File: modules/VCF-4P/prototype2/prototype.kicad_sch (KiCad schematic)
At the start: 37 parts, among them J1 Conn_01x09, U1 TL074, U2 SSI2140

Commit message: VCF-4P: prototype2 - get cutoff CV from bus
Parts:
- removed RV1: 100K, -lmp-misc:Potentiometer_Bourns_3310R_Top, symbol -lmp:R_POT_TRIM
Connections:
- net BUS-CV: now also R1.1
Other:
- note added: "TODO: Increase this to see if it fixes square wave resonance"
- note removed: "TODO: Adjust for gain & overdrive"
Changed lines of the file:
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@@
-    (stroke (width 0) (type default) (color 0 0 0 0))
-  )
-  (wire (pts (xy 39.37 137.16) (xy 39.37 138.43))
     (stroke (width 0) (type default) (color 0 0 0 0))
   )
@@
   )
   (wire (pts (xy 100.33 58.42) (xy 100.33 59.69))
-    (stroke (width 0) (type default) (color 0 0 0 0))
-  )
-  (wire (pts (xy 39.37 146.05) (xy 39.37 147.32))
     (stroke (width 0) (type default) (color 0 0 0 0))
   )
@@
     (effects (font (size 1.27 1.27)) (justify left bottom))
   )
-  (text "TODO: Adjust for \ngain & overdrive" (at 67.31 33.02 0)
+  (text "TODO: Increase this \nto see if it fixes \nsquare wave resonance"
+    (at 67.31 33.02 0)
     (effects (font (size 1.27 1.27)) (justify left bottom))
   )
@@
     (effects (font (size 1.27 1.27)) (justify left bottom))
   )
-  (global_label "BUS-CV" (shape bidirectional) (at 134.62 88.9 0) (fields_autoplaced)
+  (global_label "BUS-CV" (shape output) (at 134.62 88.9 0) (fields_autoplaced)
     (effects (font (size 1.27 1.27)) (justify left))
-    (property "Intersheet References" "${INTERSHEET_REFS}" (id 0) (at 7.62 3.81 0)
-      (effects (font (size 1.27 1.27)) hide)
-    )
-  )
-  (global_label "BUS-GATE" (shape bidirectional) (at 134.62 86.36 0) (fields_autoplaced)
+    (property "Intersheet References" "${INTERSHEET_REFS}" (id 0) (at 144.6852 88.8206 0)
+      (effects (font (size 1.27 1.27)) (justify left) hide)
+    )
+  )
+  (global_label "BUS-GATE" (shape output) (at 134.62 86.36 0) (fields_autoplaced)
     (effects (font (size 1.27 1.27)) (justify left))
-    (property "Intersheet References" "${INTERSHEET_REFS}" (id 0) (at 7.62 3.81 0)
-      (effects (font (size 1.27 1.27)) hide)
+    (property "Intersheet References" "${INTERSHEET_REFS}" (id 0) (at 146.8018 86.2806 0)
+      (effects (font (size 1.27 1.27)) (justify left) hide)
     )
   )
@@
     (effects (font (size 1.27 1.27)) (justify right))
     (property "Intersheet References" "${INTERSHEET_REFS}" (id 0) (at 27.1277 39.2906 0)
+      (effects (font (size 1.27 1.27)) (justify right) hide)
+    )
+  )
+  (global_label "BUS-CV" (shape input) (at 43.18 142.24 180) (fields_autoplaced)
+    (effects (font (size 1.27 1.27)) (justify right))
+    (property "Intersheet References" "${INTERSHEET_REFS}" (id 0) (at 33.1148 142.1606 0)
       (effects (font (size 1.27 1.27)) (justify right) hide)
     )
@@
     (pin "11")
     (pin "4")
-  )
-  (symbol (lib_id "-lmp:R_POT_TRIM") (at 39.37 142.24 0) (mirror x) (unit 1)
-    (in_bom yes) (on_board yes) (fields_autoplaced)
-    (property "Reference" "RV1" (id 0) (at 37.5921 140.1369 0)
-      (effects (font (size 1.27 1.27)) (justify right))
-    )
-    (property "Value" "100K" (id 1) (at 37.5921 142.6738 0)
-      (effects (font (size 1.27 1.27)) (justify right))
-    )
-    (property "Footprint" "-lmp-misc:Potentiometer_Bourns_3310R_Top" (id 2) (at 39.37 142.24 0)
-      (effects (font (size 1.27 1.27)) hide)
-    )
-    (property "Datasheet" "https://www.mouser.ca/datasheet/2/54/3386-776606.pdf" (id 3) (at 39.37 142.24 0)
-      (effects (font (size 1.27 1.27)) hide)
-    )
-    (property "Label" "CUTOFF" (id 4) (at 37.5921 145.2107 0)
-      (effects (font (size 1.27 1.27)) (justify right))
-    )
-    (property "Manufacturer" "Bourns" (id 5) (at 39.37 142.24 0)
-      (effects (font (size 1.27 1.27)) hide)
-    )
-    (property "ManufacturerPartNum" "3386*" (id 6) (at 39.37 142.24 0)
-      (effects (font (size 1.27 1.27)) hide)
-    )
-    (property "Distributor" "Mouser" (id 7) (at 39.37 142.24 0)
-      (effects (font (size 1.27 1.27)) hide)
-    )
-    (property "DistributorPartNum" "652-3386*" (id 8) (at 39.37 142.24 0)
-      (effects (font (size 1.27 1.27)) hide)
-    )
-    (property "DistributorPartLink" "https://www.mouser.ca/c/passive-components/resistors/variable-resistors/trimmer-resistors-through-hole/?number+of+turns=1&series=3386&instock=y" (id 9) (at 39.37 142.24 0)
-      (effects (font (size 1.27 1.27)) hide)
-    )
-    (pin "1")
-    (pin "2")
-    (pin "3")
   )
   (symbol (lib_id "-lmp:R_1%_0W166") (at 198.12 107.95 0) (unit 1)
@@
     (pin "2")
   )
-  (symbol (lib_id "-lmp-power:+12V") (at 39.37 137.16 0) (unit 1)
-    (in_bom yes) (on_board yes) (fields_autoplaced)
-    (property "Reference" "#PWR07" (id 0) (at 39.37 140.97 0)
-      (effects (font (size 1.27 1.27)) hide)
-    )
-    (property "Value" "+12V" (id 1) (at 39.37 133.5842 0))
-    (property "Footprint" "" (id 2) (at 39.37 137.16 0)
-      (effects (font (size 1.27 1.27)) hide)
-    )
-    (property "Datasheet" "" (id 3) (at 39.37 137.16 0)
-      (effects (font (size 1.27 1.27)) hide)
-    )
-    (pin "1")
-  )
   (symbol (lib_id "-lmp-power:GND") (at 121.92 148.59 0) (unit 1)
     (in_bom yes) (on_board yes) (fields_autoplaced)
@@
     (pin "1")
     (pin "2")
-  )
-  (symbol (lib_id "-lmp-power:GND") (at 39.37 147.32 0) (unit 1)
-    (in_bom yes) (on_board yes) (fields_autoplaced)
-    (property "Reference" "#PWR08" (id 0) (at 39.37 153.67 0)
-      (effects (font (size 1.27 1.27)) hide)
-    )
-    (property "Value" "GND" (id 1) (at 39.37 151.7634 0))
-    (property "Footprint" "" (id 2) (at 39.37 147.32 0)
-      (effects (font (size 1.27 1.27)) hide)
-    )
-    (property "Datasheet" "" (id 3) (at 39.37 147.32 0)
-      (effects (font (size 1.27 1.27)) hide)
-    )
-    (pin "1")
   )
   (symbol (lib_id "-lmp-synth:SSI2140") (at 222.25 41.91 0) (unit 4)
@@
       (reference "#PWR06") (unit 1) (value "-12V") (footprint "")
     )
-    (path "/71142ee8-9f39-4bb4-b70d-32261bf87f71"
-      (reference "#PWR07") (unit 1) (value "+12V") (footprint "")
-    )
-    (path "/96bd24d1-a18b-4fe1-bb89-18daf1bebf18"
-      (reference "#PWR08") (unit 1) (value "GND") (footprint "")
-    )
     (path "/84d56833-5712-4fbf-9196-b496586e82ab"
       (reference "#PWR09") (unit 1) (value "+12V") (footprint "")
@@
       (reference "R26") (unit 1) (value "10K") (footprint "-lmp-stripboard:SB_Gen_2")
     )
-    (path "/11baca3c-c206-4892-9f9f-c61e2f2a6c00"
-      (reference "RV1") (unit 1) (value "100K") (footprint "-lmp-misc:Potentiometer_Bourns_3310R_Top")
-    )
     (path "/3d155eaf-f195-466b-907a-c2cc1c99b6ea"

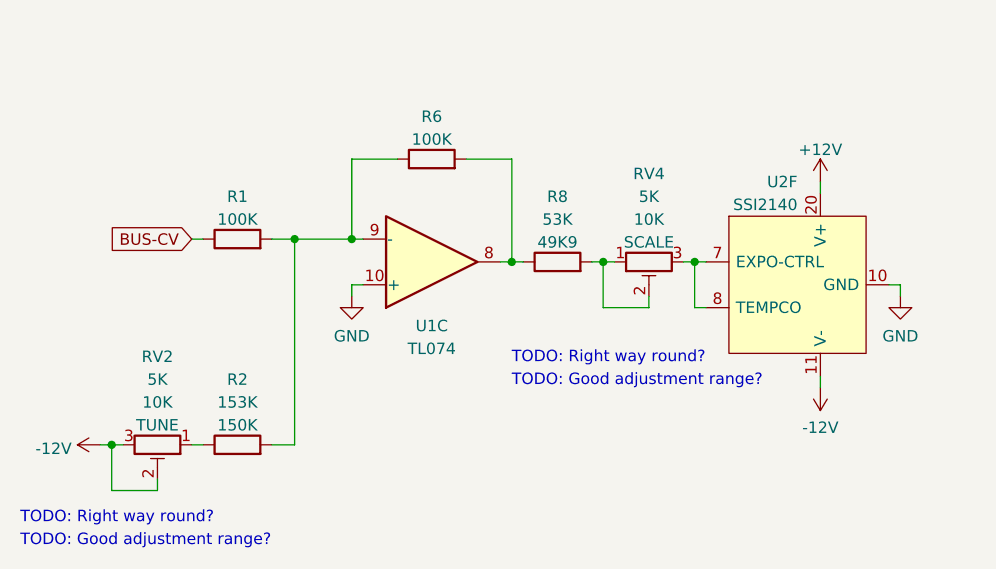
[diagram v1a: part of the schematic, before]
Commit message: VCF-4P: Calibration adjustments
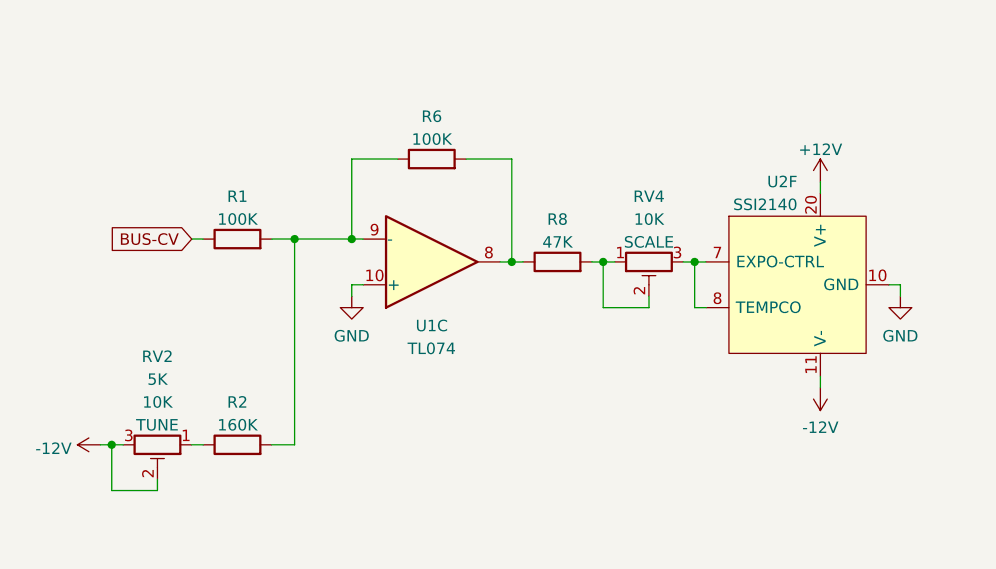
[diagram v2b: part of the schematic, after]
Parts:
- R2: value 153K -> 160K; Value2 150K -> (none)
- R8: value 53K -> 47K; Value2 49K9 -> (none)
- RV4: value 5K -> 10K; Value2 10K -> (none)
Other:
- note removed: "TODO: Good adjustment range?"
- note removed: "TODO: Right way round?"
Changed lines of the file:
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@@
     (stroke (width 0) (type default) (color 0 0 0 0))
-  )
-  (text "TODO: Good adjustment range?" (at 24.13 176.53 0)
-    (effects (font (size 1.27 1.27)) (justify left bottom))
-  )
-  (text "TODO: Right way round?" (at 78.74 156.21 0)
-    (effects (font (size 1.27 1.27)) (justify left bottom))
-  )
-  (text "TODO: Good adjustment range?" (at 78.74 158.75 0)
-    (effects (font (size 1.27 1.27)) (justify left bottom))
   )
   (text "TODO: Increase this \nto see if it fixes \nsquare wave resonance"
     (at 67.31 33.02 0)
-    (effects (font (size 1.27 1.27)) (justify left bottom))
-  )
-  (text "TODO: Right way round?" (at 24.13 173.99 0)
     (effects (font (size 1.27 1.27)) (justify left bottom))
   )
@@
   (symbol (lib_id "-lmp:R_1%_0W166") (at 83.82 144.78 90) (unit 1)
     (in_bom yes) (on_board yes) (fields_autoplaced)
-    (property "Reference" "R8" (id 0) (at 83.82 137.5274 90))
-    (property "Value" "53K" (id 1) (at 83.82 140.0643 90))
+    (property "Reference" "R8" (id 0) (at 83.82 140.0642 90))
+    (property "Value" "47K" (id 1) (at 83.82 142.6011 90))
     (property "Footprint" "-lmp-misc:R_Axial_DIN0207_L6.3mm_D2.5mm_P7.62mm_Horizontal" (id 2) (at 83.82 146.558 90)
       (effects (font (size 1.27 1.27)) hide)
@@
       (effects (font (size 1.27 1.27)) hide)
     )
-    (property "Value2" "49K9" (id 9) (at 83.82 142.6012 90))
     (pin "1")
     (pin "2")
@@
   (symbol (lib_id "-lmp:R_POT_TRIM") (at 93.98 144.78 90) (mirror x) (unit 1)
     (in_bom yes) (on_board yes) (fields_autoplaced)
-    (property "Reference" "RV4" (id 0) (at 93.98 134.9904 90))
-    (property "Value" "5K" (id 1) (at 93.98 137.5273 90))
+    (property "Reference" "RV4" (id 0) (at 93.98 137.5274 90))
+    (property "Value" "10K" (id 1) (at 93.98 140.0643 90))
     (property "Footprint" "-lmp-misc:Potentiometer_Bourns_3310R_Top" (id 2) (at 93.98 144.78 0)
       (effects (font (size 1.27 1.27)) hide)
@@
       (effects (font (size 1.27 1.27)) hide)
     )
-    (property "Value2" "10K" (id 10) (at 93.98 140.0642 90))
-    (property "Label" "SCALE" (id 4) (at 93.98 142.6011 90))
+    (property "Label" "SCALE" (id 4) (at 93.98 142.6012 90))
     (property "Manufacturer" "Bourns" (id 5) (at 93.98 144.78 0)
       (effects (font (size 1.27 1.27)) hide)
@@
   (symbol (lib_id "-lmp:R_1%_0W166") (at 48.26 165.1 90) (unit 1)
     (in_bom yes) (on_board yes) (fields_autoplaced)
-    (property "Reference" "R2" (id 0) (at 48.26 157.8474 90))
-    (property "Value" "153K" (id 1) (at 48.26 160.3843 90))
+    (property "Reference" "R2" (id 0) (at 48.26 160.3842 90))
+    (property "Value" "160K" (id 1) (at 48.26 162.9211 90))
     (property "Footprint" "-lmp-misc:R_Axial_DIN0207_L6.3mm_D2.5mm_P7.62mm_Horizontal" (id 2) (at 48.26 166.878 90)
       (effects (font (size 1.27 1.27)) hide)
@@
       (effects (font (size 1.27 1.27)) hide)
     )
-    (property "Value2" "150K" (id 9) (at 48.26 162.9212 90))
     (pin "1")
     (pin "2")
@@
     )
     (path "/5f9ab64b-38ff-4889-9d59-ea8e53307840"
-      (reference "R2") (unit 1) (value "153K") (footprint "-lmp-misc:R_Axial_DIN0207_L6.3mm_D2.5mm_P7.62mm_Horizontal")
+      (reference "R2") (unit 1) (value "160K") (footprint "-lmp-misc:R_Axial_DIN0207_L6.3mm_D2.5mm_P7.62mm_Horizontal")
     )
     (path "/f3ba663e-8563-4c48-a8cc-72c18d8d96e8"
@@
     )
     (path "/12d6a295-8009-45c3-9208-aeaaa1a487b4"
-      (reference "R8") (unit 1) (value "53K") (footprint "-lmp-misc:R_Axial_DIN0207_L6.3mm_D2.5mm_P7.62mm_Horizontal")
+      (reference "R8") (unit 1) (value "47K") (footprint "-lmp-misc:R_Axial_DIN0207_L6.3mm_D2.5mm_P7.62mm_Horizontal")
     )
     (path "/7d663747-be0a-44a3-95d5-3d1f42f6eece"
@@
     )
     (path "/48ec5117-ddfb-4cd4-89f6-ce01a6699f22"
-      (reference "RV4") (unit 1) (value "5K") (footprint "-lmp-misc:Potentiometer_Bourns_3310R_Top")
+      (reference "RV4") (unit 1) (value "10K") (footprint "-lmp-misc:Potentiometer_Bourns_3310R_Top")
     )
     (path "/0d439aa8-8969-4698-9c32-7041f6e45f4c"

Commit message: VCF-4P: prototype2 - wip
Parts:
- R3: value 1M -> 100K
- R7: Value2 15K -> 47K
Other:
- note added: "TODO: Try 30-36K with atten pot, check clipping of sq.wave w/resonance."
- note removed: "TODO: Increase this to see if it fixes square wave resonance"
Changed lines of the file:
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@@
     (stroke (width 0) (type default) (color 0 0 0 0))
   )
-  (text "TODO: Increase this \nto see if it fixes \nsquare wave resonance"
-    (at 67.31 33.02 0)
+  (text "TODO: Try 30-36K with \natten pot, check clipping \nof sq.wave w/resonance."
+    (at 64.77 33.02 0)
     (effects (font (size 1.27 1.27)) (justify left bottom))
   )
@@
       (effects (font (size 1.27 1.27)) hide)
     )
-    (property "Value2" "15K" (id 9) (at 72.39 39.7312 90))
+    (property "Value2" "47K" (id 9) (at 72.39 39.7312 90))
     (pin "1")
     (pin "2")
@@
       (effects (font (size 1.27 1.27)) (justify left))
     )
-    (property "Value" "1M" (id 1) (at 42.418 46.1522 0)
+    (property "Value" "100K" (id 1) (at 42.418 46.1522 0)
       (effects (font (size 1.27 1.27)) (justify left))
     )
@@
     )
     (path "/f3ba663e-8563-4c48-a8cc-72c18d8d96e8"
-      (reference "R3") (unit 1) (value "1M") (footprint "-lmp-stripboard:SB_Gen_1")
+      (reference "R3") (unit 1) (value "100K") (footprint "-lmp-stripboard:SB_Gen_1")
     )
     (path "/0799aeaf-0b61-4214-a215-e0119c54fb0e"

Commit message: VCF-4P: prototype2 - add input level control
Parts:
- added RV1: 100K, -lmp-misc:Potentiometer_Bourns_3310R_Top, symbol -lmp:R_POT_TRIM
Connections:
- net GND: now also RV1.1
- net at U1.3 (+): now also RV1.2; no longer C1.2
- new net: C1.2, RV1.3
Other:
- note added: "TODO: Try 30-36K with atten pot. Check clipping of sq.wave w/resonance."
- note removed: "TODO: Try 30-36K with atten pot, check clipping of sq.wave w/resonance."
- moved on the sheet: C1, C2, C3, C4, C5, J1, R1, R10, R11, R12, R13, R14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
